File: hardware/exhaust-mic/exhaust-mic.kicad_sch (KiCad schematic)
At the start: 0 parts

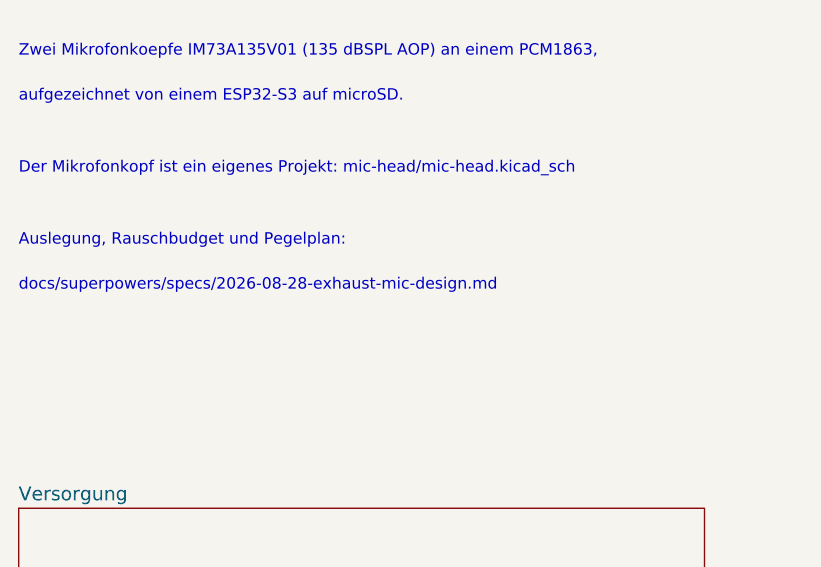
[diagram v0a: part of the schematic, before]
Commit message: Spezifikation nach docs/specs verschieben und Verweise nachziehen
Der bisherige Pfad enthielt ein Verzeichnis, dessen Name nichts mit dem
Projekt zu tun hat. Er stand an sechs Stellen, darunter als Text auf dem
Schaltplanblatt - die beiden Schaltplan-PDF sind deshalb neu erzeugt.

Die vier mitgeaenderten Dateien unter hardware/exhaust-mic lagen hier auf
einem alten Stand; sie kommen jetzt auf den des exhaust-mic-Repos. Die
uebrigen Dateien dort bleiben unberuehrt und weiterhin veraltet.
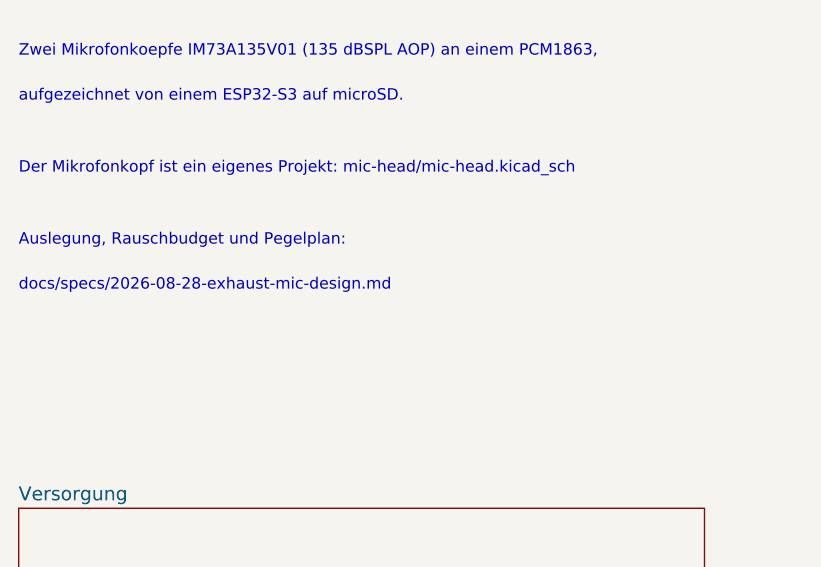
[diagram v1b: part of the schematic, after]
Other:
- note added: "docs/specs/2026-08-28-exhaust-mic-design.md"
- note removed: "docs/superpowers/specs/2026-08-28-exhaust-mic-design.md"
- company: Hayabusa / exhaust-mic -> (none)
